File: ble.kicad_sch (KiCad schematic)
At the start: 8 parts, among them Y2 FC-135 32.7680KA-AC0

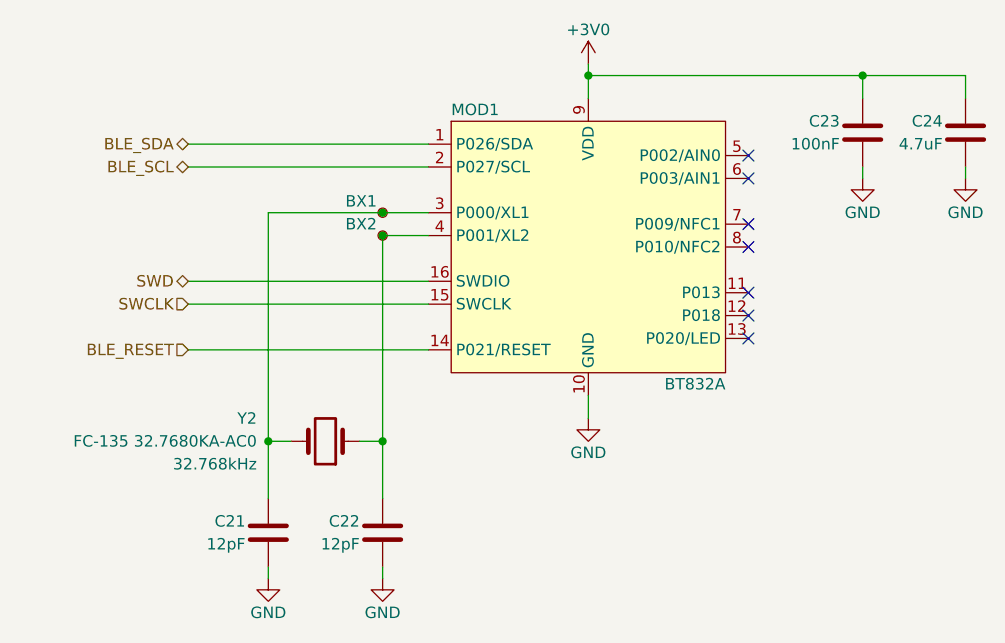
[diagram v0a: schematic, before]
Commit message: pcb done, also kicad 8
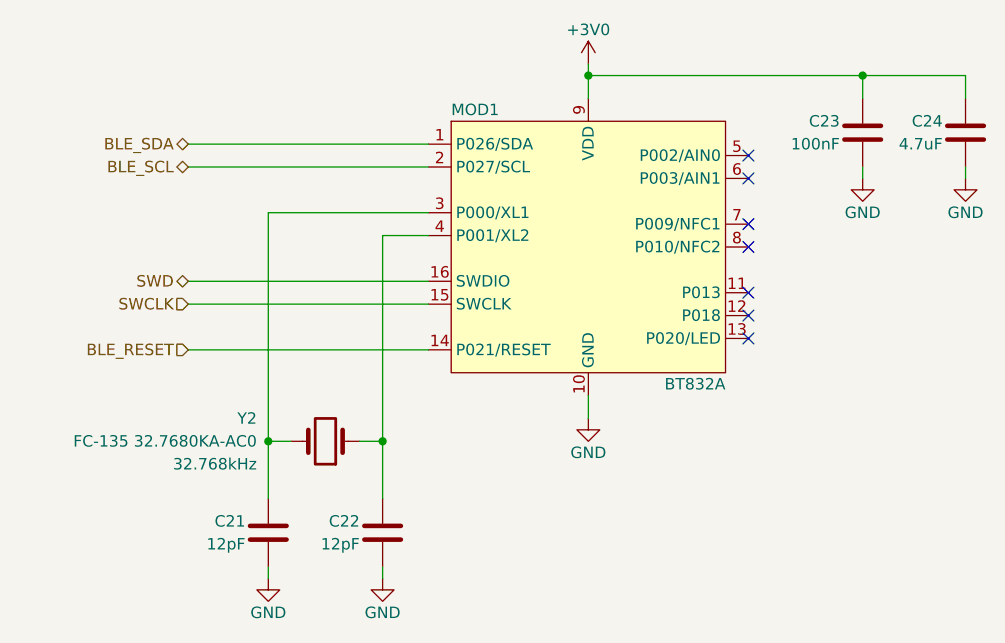
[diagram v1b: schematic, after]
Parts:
- removed TP48: BX1, TestPoint:TestPoint_Pad_D1.0mm, symbol Connector:TestPoint_Small
- removed TP49: BX2, TestPoint:TestPoint_Pad_D1.0mm, symbol Connector:TestPoint_Small
